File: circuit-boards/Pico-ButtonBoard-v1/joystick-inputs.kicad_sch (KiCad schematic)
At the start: 25 parts, among them J25 XY0-R, J26 XY1-L, U7 MCP3201T-CI/SN, U9 MCP1700T-3302E/TT

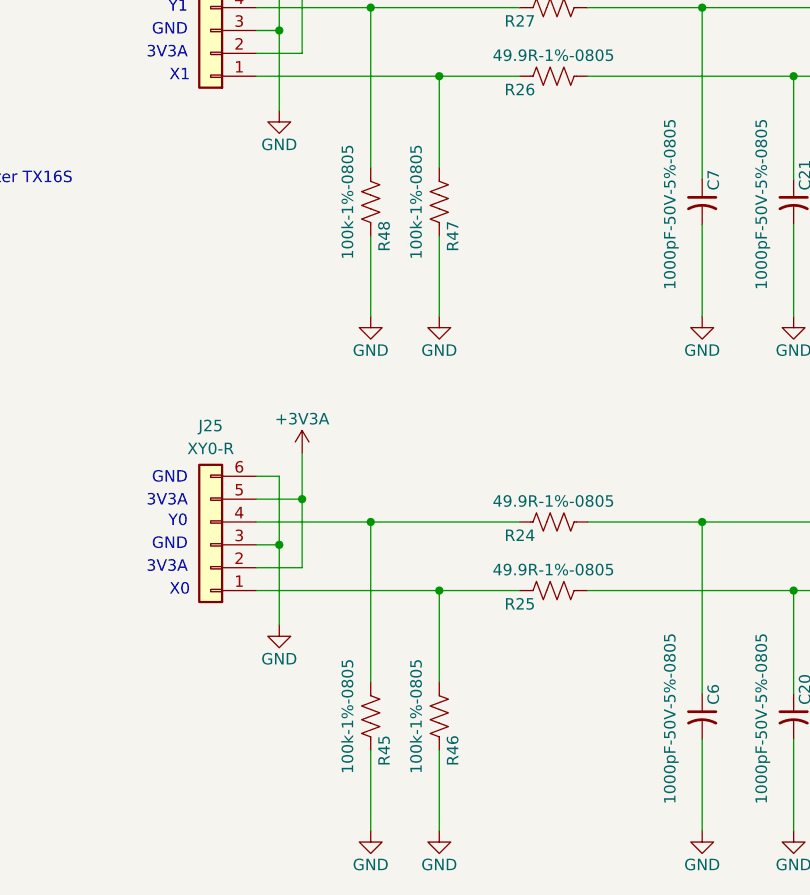
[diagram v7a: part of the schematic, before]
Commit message: DNP joystick pull down resistors
Signed-off-by: Scott Berman <sgberman1@gmail.com>
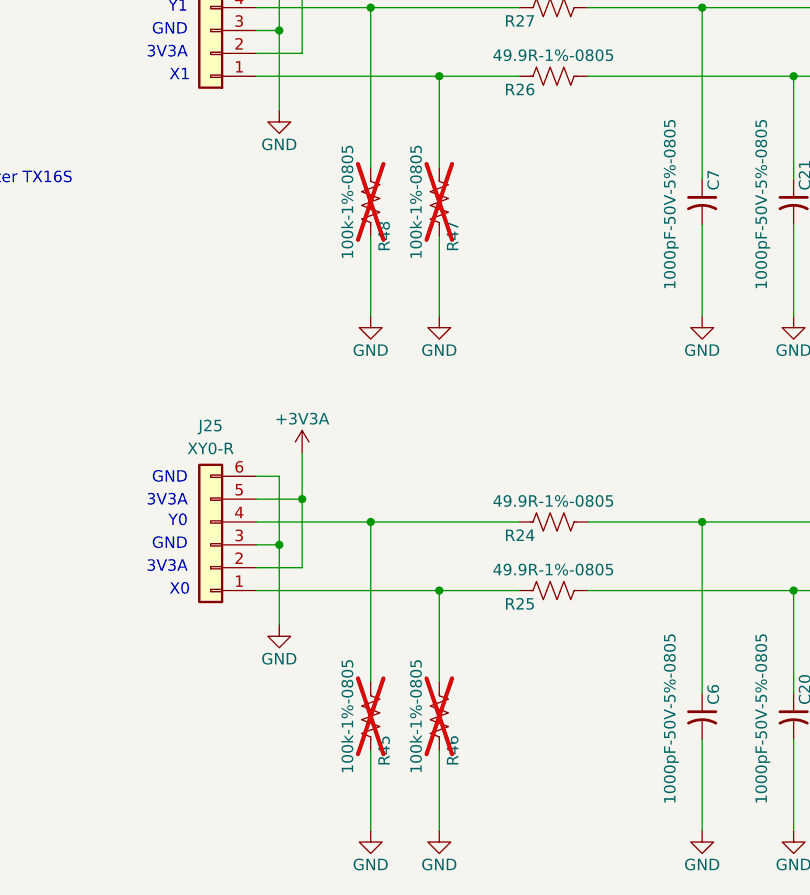
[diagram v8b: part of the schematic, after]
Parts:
- R45, R46, R47, R48: now not fitted
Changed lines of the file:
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@@
 		(in_bom yes)
 		(on_board yes)
-		(dnp no)
+		(dnp yes)
 		(property "Reference" "R48"
 			(at 129.794 171.45 90)
@@
 		(in_bom yes)
 		(on_board yes)
-		(dnp no)
+		(dnp yes)
 		(property "Reference" "R46"
 			(at 137.414 228.6 90)
@@
 		(in_bom yes)
 		(on_board yes)
-		(dnp no)
+		(dnp yes)
 		(property "Reference" "R47"
 			(at 137.414 171.45 90)
@@
 		(in_bom yes)
 		(on_board yes)
-		(dnp no)
+		(dnp yes)
 		(property "Reference" "R45"
 			(at 129.794 228.6 90)
